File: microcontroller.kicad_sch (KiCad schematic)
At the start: 1 part, among them U1 STM32H745XIH6

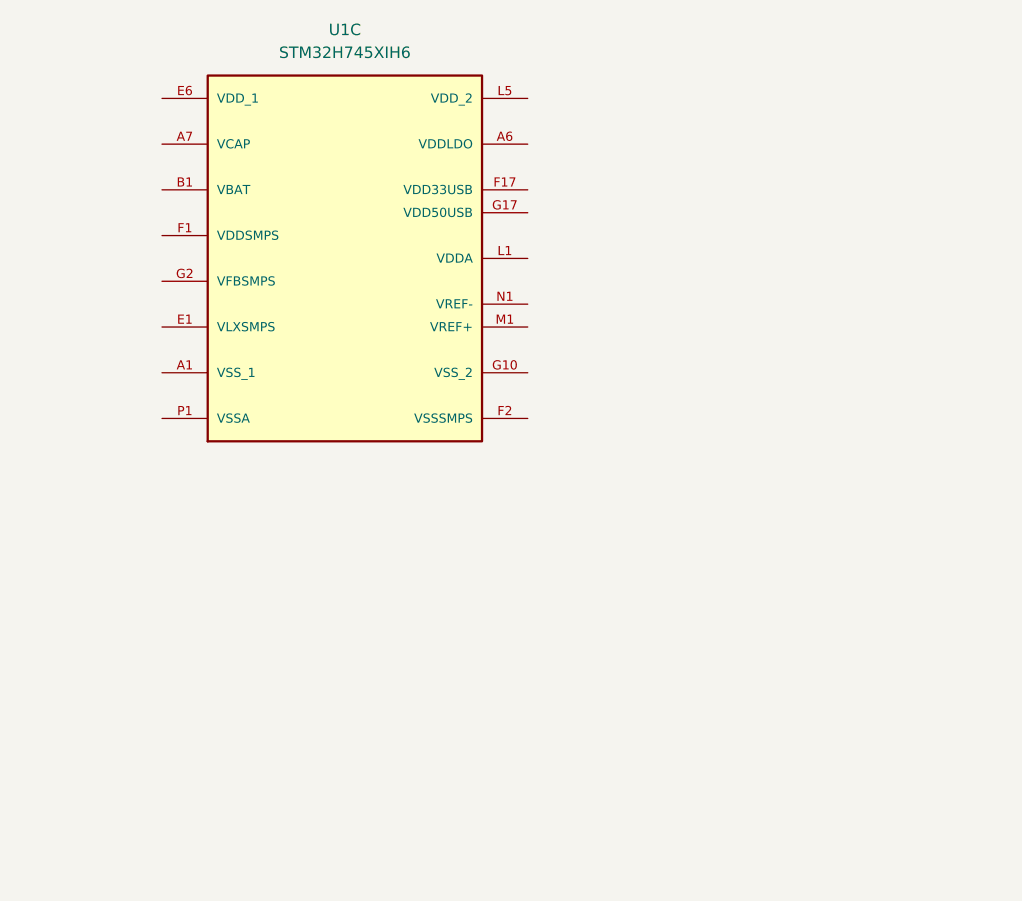
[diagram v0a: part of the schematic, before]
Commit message: add microcontroller decoupling
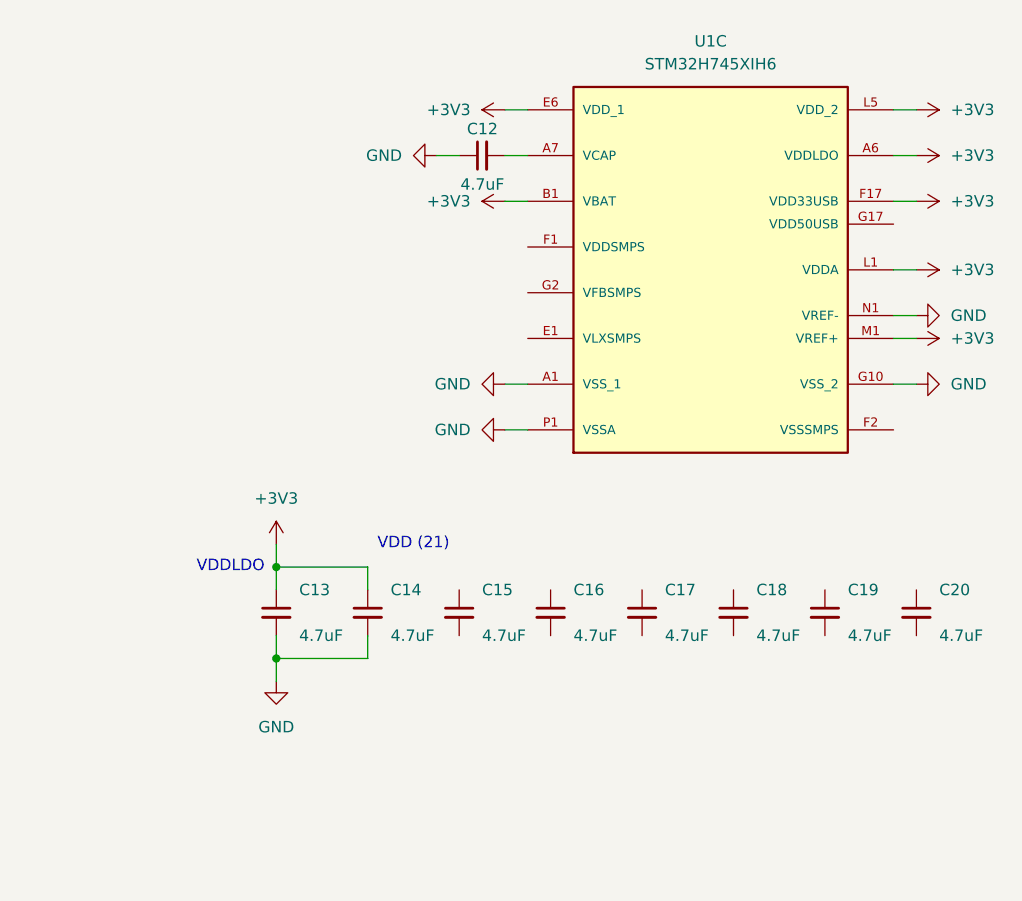
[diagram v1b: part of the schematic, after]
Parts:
- added C12, C13, C14, C15, C16, C17, C18, C19, C20: 4.7uF, Capacitor_SMD:C_0402_1005Metric, symbol Device:C_Small
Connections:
- net VDDLDO is gone; now on net +3V3: U1.A6 (VDDLDO), U1.C17 (VDDLDO), U1.U12 (VDDLDO)
- net VDD_1 is gone; now on net +3V3: U1.E11 (VDD_1), U1.E6 (VDD_1), U1.E9 (VDD_1), U1.F5 (VDD_1), U1.G13 (VDD_1), U1.G5 (VDD_1), U1.H13 (VDD_1), U1.H5 (VDD_1), U1.J13 (VDD_1), U1.K13 (VDD_1), U1.K5 (VDD_1)
- net VDD_2 is gone; now on net +3V3: U1.L13 (VDD_2), U1.L5 (VDD_2), U1.M13 (VDD_2), U1.M5 (VDD_2), U1.N10 (VDD_2), U1.N11 (VDD_2), U1.N12 (VDD_2), U1.N7 (VDD_2), U1.N8 (VDD_2), U1.P17 (VDD_2)
- net VSS_1 is gone; now on net GND: U1.A1 (VSS_1), U1.A17 (VSS_1), U1.B2 (VSS_1), U1.B6 (VSS_1), U1.C10 (VSS_1), U1.C13 (VSS_1), U1.C16 (VSS_1), U1.G16 (VSS_1), U1.G7 (VSS_1), U1.G8 (VSS_1), U1.G9 (VSS_1), U1.J16 (VSS_1), U1.J17 (VSS_1), U1.J3 (VSS_1), U1.K15 (VSS_1), U1.L15 (VSS_1), U1.M15 (VSS_1), U1.N16 (VSS_1), U1.R4 (VSS_1), U1.R8 (VSS_1), U1.T12 (VSS_1), U1.U1 (VSS_1), U1.U17 (VSS_1)
- net VSS_2 is gone; now on net GND: U1.G10 (VSS_2), U1.G11 (VSS_2), U1.H10 (VSS_2), U1.H11 (VSS_2), U1.H7 (VSS_2), U1.H8 (VSS_2), U1.H9 (VSS_2), U1.J10 (VSS_2), U1.J11 (VSS_2), U1.J7 (VSS_2), U1.J8 (VSS_2), U1.J9 (VSS_2), U1.K10 (VSS_2), U1.K11 (VSS_2), U1.K7 (VSS_2), U1.K8 (VSS_2), U1.K9 (VSS_2), U1.L10 (VSS_2), U1.L11 (VSS_2), U1.L7 (VSS_2), U1.L8 (VSS_2), U1.L9 (VSS_2)
- net VCAP: now also C12.2
- net +3V3: now reaches U1.B1 (VBAT)
- net +3V3: now also U1.F17 (VDD33USB), U1.L1 (VDDA), U1.M1 (VREF+), C13.1, C14.1
- net GND: now reaches U1.N1 (VREF-)
- net GND: now also U1.P1 (VSSA), C12.1, C13.2, C14.2
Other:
- note added: "VDD (21)"
- note added: "VDDLDO"
- moved on the sheet: U1C

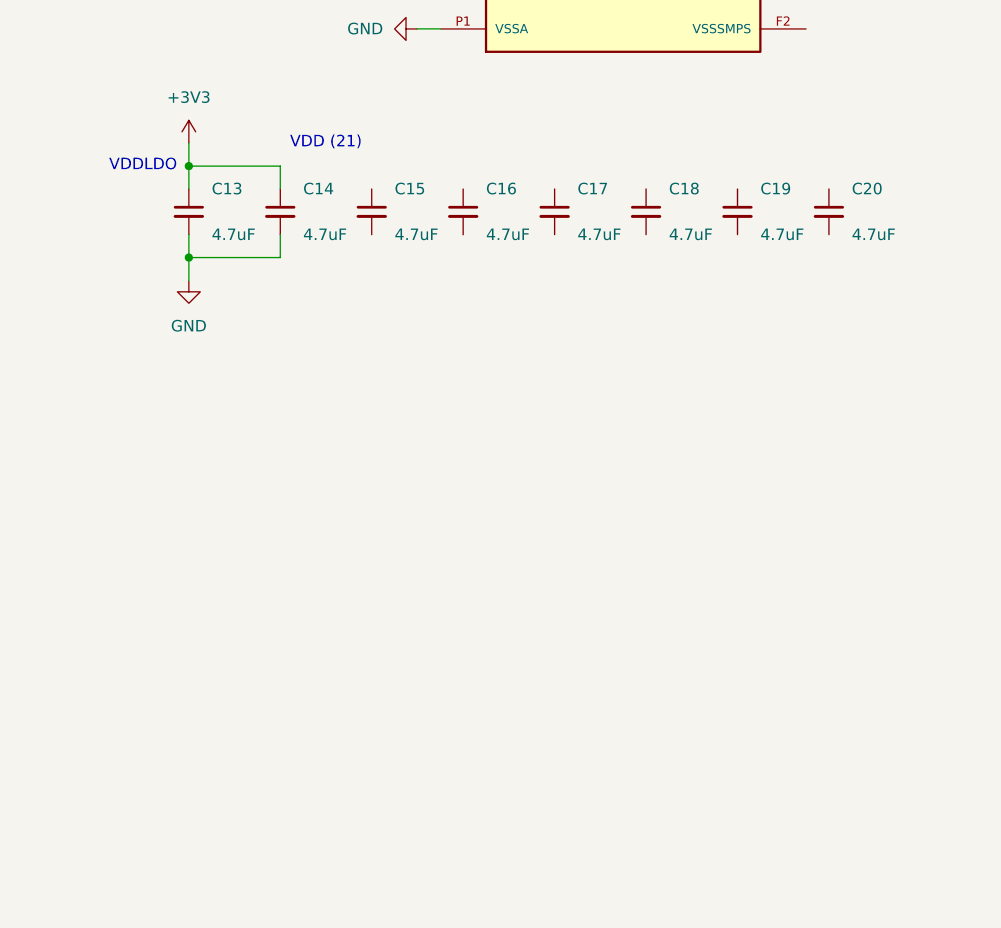
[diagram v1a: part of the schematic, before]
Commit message: add decoupling caps
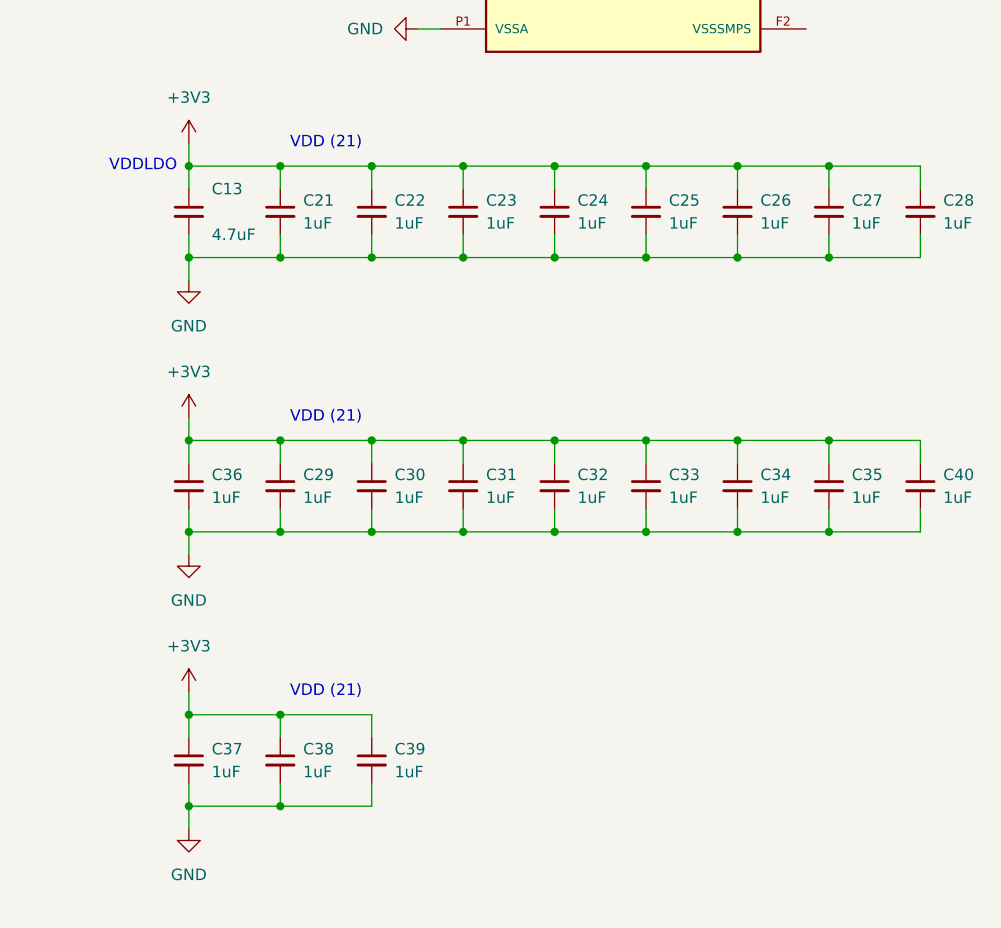
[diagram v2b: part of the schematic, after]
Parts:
- removed C14, C15, C16, C17, C18, C19, C20: 4.7uF, Capacitor_SMD:C_0402_1005Metric, symbol Device:C_Small
- added C21, C22, C23, C24, C25, C26, C27, C28, C29, C30, C31, C32, C33, C34, C35, C36, C37, C38, C39, C40: 1uF, Capacitor_SMD:C_0402_1005Metric, symbol Device:C_Small
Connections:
- net +3V3: now also C21.1, C22.1, C23.1, C24.1, C25.1, C26.1, C27.1, C28.1, C29.1, C30.1, C31.1, C32.1, C33.1, C34.1, C35.1, C36.1, C37.1, C38.1, C39.1, C40.1
- net GND: now also C21.2, C22.2, C23.2, C24.2, C25.2, C26.2, C27.2, C28.2, C29.2, C30.2, C31.2, C32.2, C33.2, C34.2, C35.2, C36.2, C37.2, C38.2, C39.2, C40.2

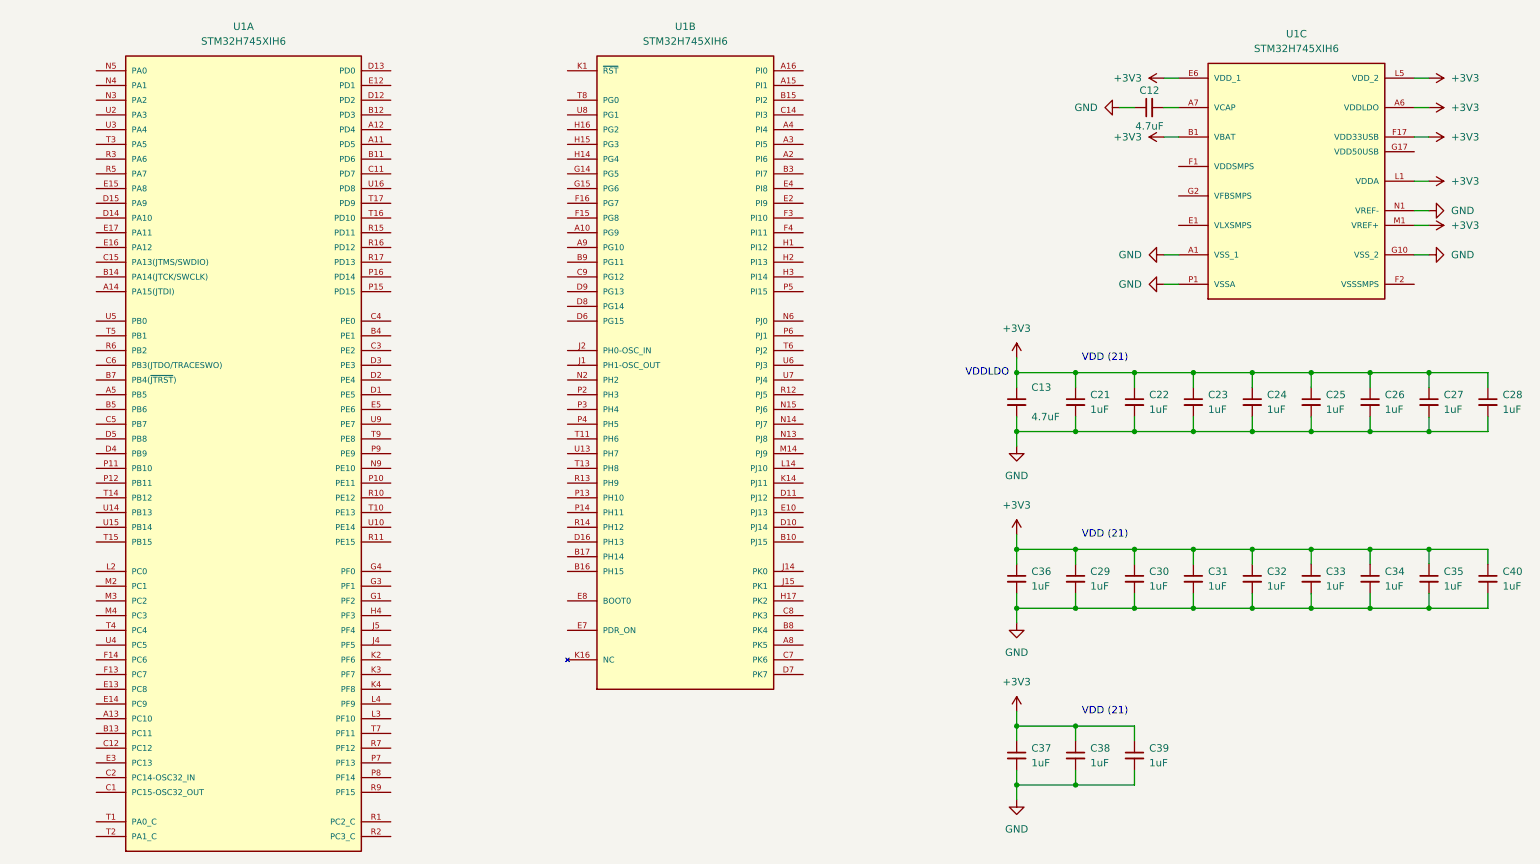
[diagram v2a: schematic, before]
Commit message: fix footprints and add smps
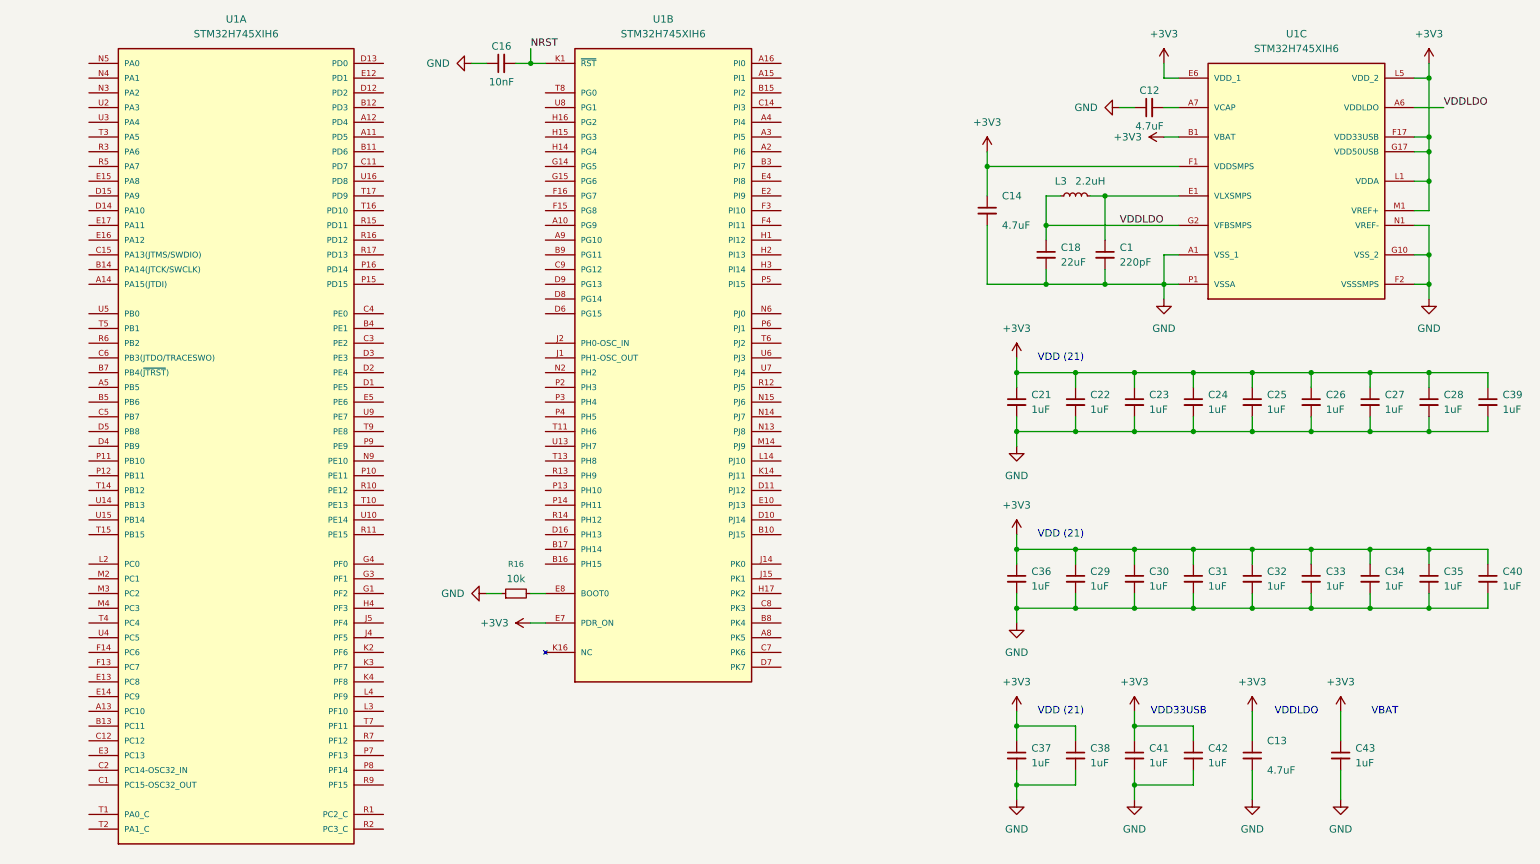
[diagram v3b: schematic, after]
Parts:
- added C1: 220pF, Capacitor_SMD:C_0402_1005Metric, symbol Device:C_Small
- added C14: 4.7uF, Capacitor_SMD:C_0402_1005Metric, symbol Device:C_Small
- added C16: 10nF, Capacitor_SMD:C_0402_1005Metric, symbol Device:C_Small
- added C18: 22uF, Capacitor_SMD:C_0805_2012Metric, symbol Device:C_Small
- added C41, C42, C43: 1uF, Capacitor_SMD:C_0402_1005Metric, symbol Device:C_Small
- added L3: 2.2uH, Inductor_SMD:L_0805_2012Metric, symbol Device:L_Small
- added R16: 10k, Resistor_SMD:R_0402_1005Metric, symbol Device:R_Small
- U1: footprint footprints:BGA265C80P17X17_1400X1400X120 -> STM32H745XIH6:BGA265C80P17X17_1400X1400X120; symbol symbols:STM32H745XIH6 -> custom:STM32H745XIH6
- U1: footprint footprints:BGA265C80P17X17_1400X1400X120 -> custom:BGA265C80P17X17_1400X1400X120
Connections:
- net +3V3: now also U1.E7 (PDR_ON), U1.F1 (VDDSMPS), U1.G17 (VDD50USB), C14.1, C41.1, C42.1, C43.1; no longer U1.A6 (VDDLDO), U1.C17 (VDDLDO), U1.U12 (VDDLDO)
- net GND: now also U1.F2 (VSSSMPS), C1.2, C14.2, C16.1, C18.2, C41.2, C42.2, C43.2, R16.1
- net at U1.E1 (VLXSMPS): now also C1.1, L3.2
- net VDDLDO: now reaches U1.G2 (VFBSMPS)
- net VDDLDO: now also U1.A6 (VDDLDO), U1.C17 (VDDLDO), U1.U12 (VDDLDO), C18.1, L3.1
- net at U1.E8 (BOOT0): now also R16.2
- net NRST: now reaches U1.K1 (~{RST})
- net NRST: now also C16.2
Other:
- note added: "VBAT"
- note added: "VDD33USB"
- moved on the sheet: C13, C21, C22, C23, C24, C25, C26, C27, C28, U1A, U1B

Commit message: add user led
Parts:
- added D2: LED, LED_SMD:LED_0402_1005Metric, symbol Device:LED
- added R17: 15k, Resistor_SMD:R_0402_1005Metric, symbol Device:R_Small
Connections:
- net GND: now also D2.1 (K)
- net USER_LED: now reaches U1.T3 (PA5)
- net USER_LED: now also R17.2
- new net: D2.2 (A), R17.1
